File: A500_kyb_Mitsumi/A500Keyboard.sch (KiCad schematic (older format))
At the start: 34 parts, among them IC1 6570-036, IC2- 74LS27, IC3- 74LS123, IC4 NE555, J1 KYB_MATRIX, J2 Interface, Q1 BC485C, Q2 BC485C, Y1 3.000 MHz

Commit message: Kicad 5 conversion (automatic upon schematic opening): - No changes aside from the conversion were made to the files. - Added project conversion report. - Added .gitignore to avoid versioning unnecessary files and folders:   - "rescue-backup" folder generated during the Kicad5 conversion,   - backup files generated during save.
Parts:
- C1, C10, C11, C12, C13, C14, C2, C3, C4, C5, C6, C8, C9: symbol C -> Device:C
- D? (x4): symbol LED_ALT -> Device:LED_ALT
- IC1: symbol 6570-036 -> A500_Parts:6570-036
- IC2-: symbol 74LS27 -> A500Keyboard-rescue:74LS27
- IC3-: symbol 74LS123 -> A500Keyboard-rescue:74LS123
- IC4: symbol NE555 -> A500Keyboard-rescue:NE555
- J1: symbol KYB_MATRIX -> A500_Parts:KYB_MATRIX
- J2: symbol Interface -> A500_Parts:Interface
- Q1, Q2: symbol Q_NPN_ECB -> Device:Q_NPN_ECB
- R1, R10, R2, R3, R5, R6, R7, R8: symbol R -> Device:R
- Y1: symbol Crystal -> Device:Crystal
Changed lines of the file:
@@
-EESchema Schematic File Version 2
-LIBS:power
-LIBS:device
-LIBS:transistors
-LIBS:conn
-LIBS:linear
-LIBS:regul
-LIBS:74xx
-LIBS:cmos4000
-LIBS:adc-dac
-LIBS:memory
-LIBS:xilinx
-LIBS:microcontrollers
-LIBS:dsp
-LIBS:microchip
-LIBS:analog_switches
-LIBS:motorola
-LIBS:texas
-LIBS:intel
-LIBS:audio
-LIBS:interface
-LIBS:digital-audio
-LIBS:philips
-LIBS:display
-LIBS:cypress
-LIBS:siliconi
-LIBS:opto
-LIBS:atmel
-LIBS:contrib
-LIBS:valves
-LIBS:A500_Parts
-LIBS:A500Keyboard_Parts
-LIBS:A500Keyboard-cache
-EELAYER 25 0
+EESchema Schematic File Version 4
+EELAYER 30 0
 EELAYER END
 $Descr USLetter 11000 8500
@@
 $EndDescr
 $Comp
-L KYB_MATRIX J1
+L A500_Parts:KYB_MATRIX J1
 U 1 1 5A78FF17
 P 4700 2450
@@
 $EndComp
 $Comp
-L VCC #PWR?
+L power:VCC #PWR?
 U 1 1 5A7904F6
 P 1250 950
@@
 $EndComp
 $Comp
-L Crystal Y1
+L Device:Crystal Y1
 U 1 1 5A790564
 P 1100 2400
@@
 $EndComp
 $Comp
-L C C13
+L Device:C C13
 U 1 1 5A790650
 P 1100 2950
@@
 $EndComp
 $Comp
-L C C12
+L Device:C C12
 U 1 1 5A7906A2
 P 700 2950
@@
 $EndComp
 $Comp
-L GND #PWR?
+L power:GND #PWR?
 U 1 1 5A7906CF
 P 1325 5400
@@
 $EndComp
 $Comp
-L GND #PWR?
+L power:GND #PWR?
 U 1 1 5A790774
 P 900 3450
@@
 $EndComp
 $Comp
-L GND #PWR?
+L power:GND #PWR?
 U 1 1 5A7914C4
 P 5150 4150
@@
 $EndComp
 $Comp
-L VCC #PWR?
+L power:VCC #PWR?
 U 1 1 5A7919FB
 P 5150 875
@@
 $EndComp
 $Comp
-L Interface J2
+L A500_Parts:Interface J2
 U 1 1 5A7921BD
 P 3800 6900
@@
 $EndComp
 $Comp
-L 6570-036 IC1
+L A500_Parts:6570-036 IC1
 U 1 1 5A7900F4
 P 2350 3650
@@
 $EndComp
 $Comp
-L GND #PWR?
+L power:GND #PWR?
 U 1 1 5A792668
 P 3250 7500
@@
 $EndComp
 $Comp
-L VCC #PWR?
+L power:VCC #PWR?
 U 1 1 5A792794
 P 3250 6300
@@
 $EndComp
 $Comp
-L R R5
+L Device:R R5
 U 1 1 5A792885
 P 4650 6900
@@
 $EndComp
 $Comp
-L R R6
+L Device:R R6
 U 1 1 5A792959
 P 4650 7450
@@
 $EndComp
 $Comp
-L LED_ALT D?
+L Device:LED_ALT D?
 U 1 1 5A792ADB
 P 5050 6900
@@
 $EndComp
 $Comp
-L LED_ALT D?
+L Device:LED_ALT D?
 U 1 1 5A792B33
 P 5450 6900
@@
 $EndComp
 $Comp
-L LED_ALT D?
+L Device:LED_ALT D?
 U 1 1 5A792B6B
 P 5050 7450
@@
 $EndComp
 $Comp
-L LED_ALT D?
+L Device:LED_ALT D?
 U 1 1 5A792BA6
 P 5475 7450
@@
 $EndComp
 $Comp
-L GND #PWR?
+L power:GND #PWR?
 U 1 1 5A792E24
 P 5750 7600
@@
 $EndComp
 $Comp
-L R R10
+L Device:R R10
 U 1 1 5A7A6032
 P 1050 6850
@@
 $EndComp
 $Comp
-L Q_NPN_ECB Q2
+L Device:Q_NPN_ECB Q2
 U 1 1 5A7A621D
 P 1350 7250
@@
 $EndComp
 $Comp
-L GND #PWR?
+L power:GND #PWR?
 U 1 1 5A7B62F0
 P 1450 7550
@@
 PULS
 $Comp
-L R R1
+L Device:R R1
 U 1 1 5A7B723F
 P 7650 1625
@@
 $EndComp
 $Comp
-L VCC #PWR?
+L power:VCC #PWR?
 U 1 1 5A7B7428
 P 9000 1125
@@
 $EndComp
 $Comp
-L Q_NPN_ECB Q1
+L Device:Q_NPN_ECB Q1
 U 1 1 5A7B77AC
 P 7925 1900
@@
 $EndComp
 $Comp
-L GND #PWR?
+L power:GND #PWR?
 U 1 1 5A7B7A0F
 P 8025 2375
@@
 $EndComp
 $Comp
-L R R3
+L Device:R R3
 U 1 1 5A7B80F4
 P 8025 1475
@@
 $EndComp
 $Comp
-L C C9
+L Device:C C9
 U 1 1 5A7B835E
 P 8375 1900
@@
 $EndComp
 $Comp
-L NE555 IC4
+L A500Keyboard-rescue:NE555 IC4
 U 1 1 5A7B87DB
 P 9325 1875
@@
 $EndComp
 $Comp
-L C C6
+L Device:C C6
 U 1 1 5A7B8B74
 P 10375 1875
@@
 $EndComp
 $Comp
-L R R2
+L Device:R R2
 U 1 1 5A7B8F9D
 P 10050 1575
@@
 $EndComp
 $Comp
-L C C5
+L Device:C C5
 U 1 1 5A7B927F
 P 10050 2100
@@
 $EndComp
 $Comp
-L C C8
+L Device:C C8
 U 1 1 5A7B9471
 P 8625 2100
@@
 $EndComp
 $Comp
-L 74LS27 IC2-
+L A500Keyboard-rescue:74LS27 IC2-
 U 3 1 5A7B99D8
 P 9150 3175
@@
 $EndComp
 $Comp
-L 74LS27 IC2-
+L A500Keyboard-rescue:74LS27 IC2-
 U 1 1 5A7B9CF7
 P 9150 3700
@@
 PULS
 $Comp
-L 74LS123 IC3-
+L A500Keyboard-rescue:74LS123 IC3-
 U 2 1 5A7BAB90
 P 9550 5500
@@
 $EndComp
 $Comp
-L 74LS123 IC3-
+L A500Keyboard-rescue:74LS123 IC3-
 U 1 1 5A7BAC84
 P 7900 5450
@@
 $EndComp
 $Comp
-L VCC #PWR?
+L power:VCC #PWR?
 U 1 1 5A7BB49D
 P 7000 4350
@@
 NoConn ~ 8650 5750
 $Comp
-L R R7
+L Device:R R7
 U 1 1 5A7BBAD7
 P 7400 4550
@@
 $EndComp
 $Comp
-L C C2
+L Device:C C2
 U 1 1 5A7BBC07
 P 3050 7150
@@
 $EndComp
 $Comp
-L C C1
+L Device:C C1
 U 1 1 5A7BC4CD
 P 2700 7150
@@
 $EndComp
 $Comp
-L C C10
+L Device:C C10
 U 1 1 5A7BCF32
 P 7900 4550
@@
 $EndComp
 $Comp
-L VCC #PWR?
+L power:VCC #PWR?
 U 1 1 5A7BD612
 P 8725 4350
@@
 $EndComp
 $Comp
-L R R8
+L Device:R R8
 U 1 1 5A7BE17B
 P 9075 4550
@@
 $EndComp
 $Comp
-L C C11
+L Device:C C11
 U 1 1 5A7BE445
 P 9550 4550
@@
 $EndComp
 $Comp
-L 74LS27 IC2-
+L A500Keyboard-rescue:74LS27 IC2-
 U 2 1 5A791C50
 P 6975 1900
@@
 Note: Lift Q1 pin 3 to disable Ctrl-A-A A500/6500 reset
 $Comp
-L C C3
+L Device:C C3
 U 1 1 5A7ED1CA
 P 6875 3500
@@
 $EndComp
 $Comp
-L VCC #PWR?
+L power:VCC #PWR?
 U 1 1 5A7ED264
 P 7225 3175
@@
 $EndComp
 $Comp
-L GND #PWR?
+L power:GND #PWR?
 U 1 1 5A7ED2FB
 P 7225 3825
@@
 $EndComp
 $Comp
-L C C4
+L Device:C C4
 U 1 1 5A7EDB46
 P 7225 3500
@@
 $EndComp
 $Comp
-L C C14
+L Device:C C14
 U 1 1 5A7EDC3D
 P 7575 3500

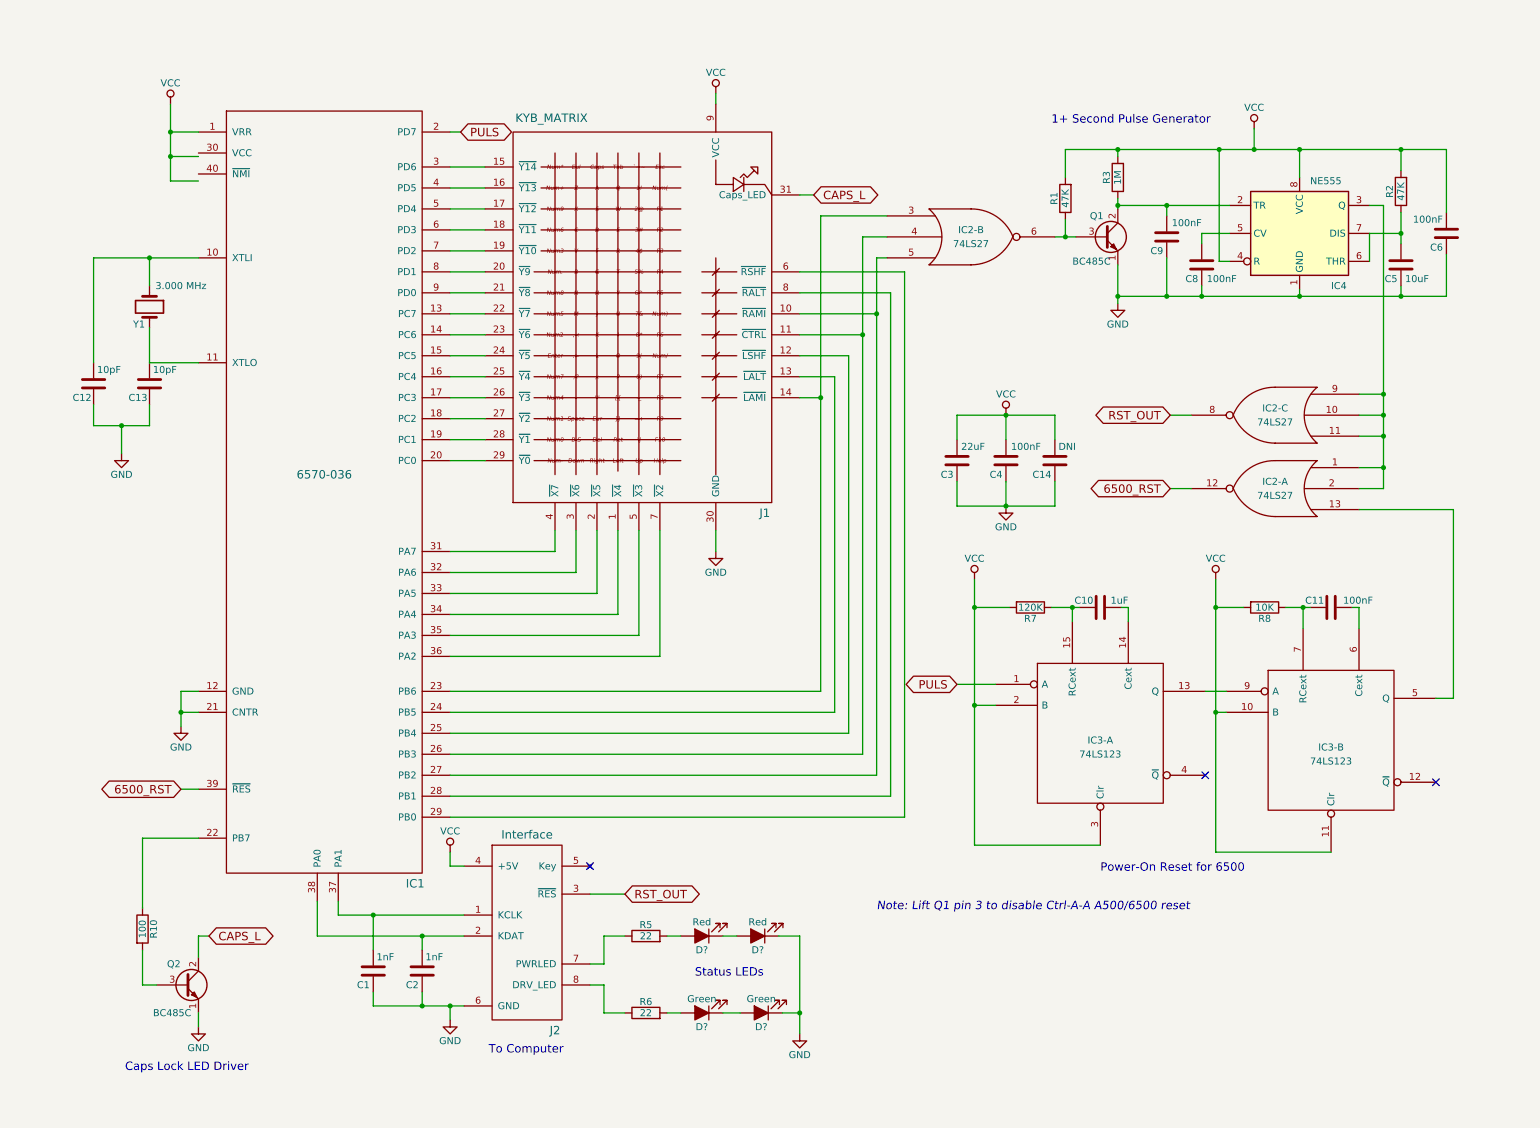
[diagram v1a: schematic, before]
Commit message: Miscellaneous small reworks: - Renamed symbols to conform to those of the official Commodore A500/A500+ schematics. - Fixed Labels to properly match their Input/Output status (they were showing as bidirectional). - Now uses a connector from the standard KiCad library. - Made the LEDs section into its own functional block away from the connector.
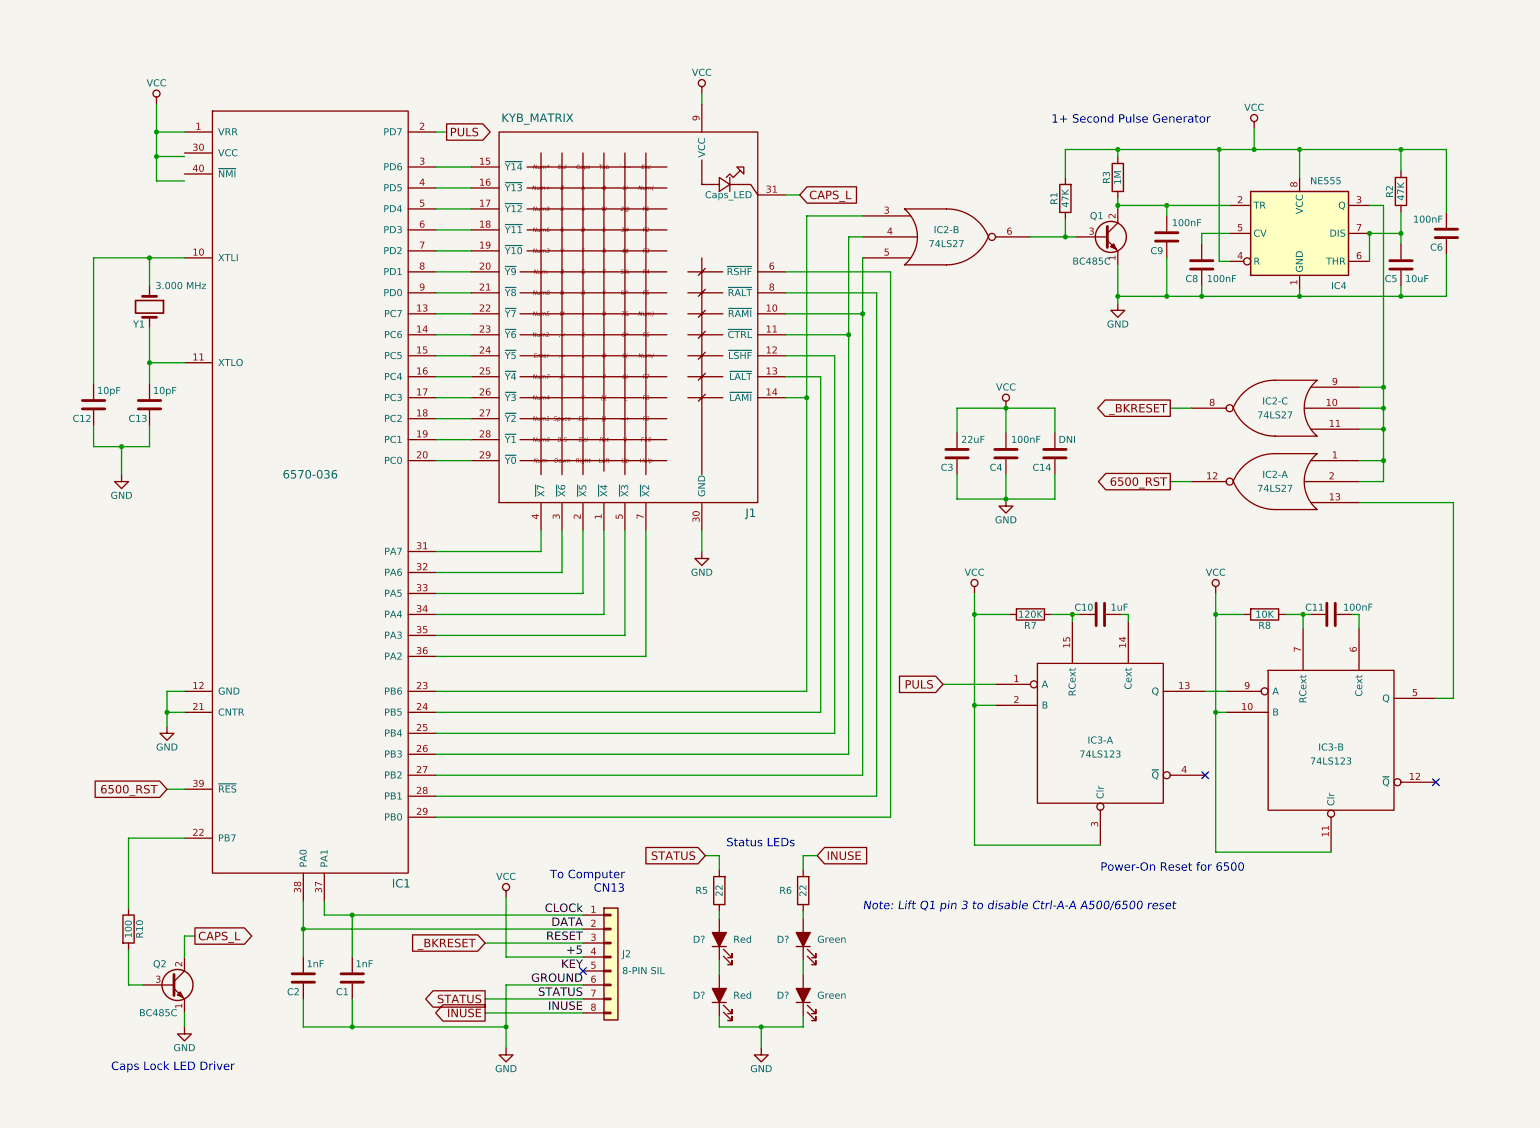
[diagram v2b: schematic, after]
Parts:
- removed J2: Interface, symbol A500_Parts:Interface
- added J2: 8-PIN SIL, symbol Connector_Generic:Conn_01x08
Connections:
- net GND: now also J2.6 (Pin_6)
- net VCC: now also J2.4 (Pin_4)
- net CLOCk: now reaches C1.2, IC1.37 (PA1)
- net CLOCk: now also J2.1 (Pin_1)
- net DATA: now reaches C2.2, IC1.38 (PA0)
- net DATA: now also J2.2 (Pin_2)
- net at R5.1: now also D?.2 (A)
- net at R6.1: now also D?.2 (A)
- net STATUS: now reaches R5.2
- net STATUS: now also J2.7 (Pin_7); no longer D?.2 (A)
- net INUSE: now reaches R6.2
- net INUSE: now also J2.8 (Pin_8); no longer D?.2 (A)
- net RST_OUT renamed _BKRESET
- net _BKRESET: now also J2.3 (Pin_3)
- new net KEY: J2.5 (Pin_5)
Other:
- note added: "To Computer\nCN13"
- note removed: "To Computer"
- moved on the sheet: C1, C10, C11, C12, C13, C14, C2, C3, C4, D?, IC1, IC2-A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
